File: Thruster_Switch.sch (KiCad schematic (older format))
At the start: 16 parts, among them P1 XT60, P2 XT60, P3 XT60, P4 XT60, Q1 BC817-40, Q2 IPD90P03P4L

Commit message: Fixed bugs from misunderstanding about Thruster, DVL, and Sonar switch biases.
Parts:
- removed C1: 1uF, Capacitors_SMD:C_0603, symbol C
- removed D1: MBR0530T3G, Diodes_SMD:D_SOD-123, symbol D
- removed Q1: BC817-40, TO_SOT_Packages_SMD:SOT-23, symbol BC817-40
- removed R1: 2.2k, Resistors_SMD:R_0603, symbol R
- removed R2: 330, Resistors_SMD:R_0603, symbol R
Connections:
- net labels removed: Hardware_Switch
- wire segments 32 -> 23
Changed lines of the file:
@@
 encoding utf-8
 Sheet 2 10
-Title ""
+Title "Thruster Switch"
 Date "2017-04-06"
 Rev "1.0.0"
@@
 L GND #PWR016
 U 1 1 58E0369B
-P 5250 4900
+P 6250 4800
 AR Path="/58E52973/58E0369B" Ref="#PWR016"  Part="1"
 AR Path="/58E62AD5/58E0369B" Ref="#PWR019"  Part="1"
 AR Path="/58E6D43E/58E0369B" Ref="#PWR020"  Part="1"
 AR Path="/58E0048C/58E0369B" Ref="#PWR021"  Part="1"
-F 0 "#PWR021" H 5250 4650 50  0001 C CNN
-F 1 "GND" H 5250 4750 50  0000 C CNN
-F 2 "" H 5250 4900 50  0001 C CNN
-F 3 "" H 5250 4900 50  0001 C CNN
-	1    5250 4900
-	1    0    0    -1
-$EndComp
-Text HLabel 3650 2300 0    60   Input ~ 0
+F 0 "#PWR016" H 6250 4550 50  0001 C CNN
+F 1 "GND" H 6250 4650 50  0000 C CNN
+F 2 "" H 6250 4800 50  0001 C CNN
+F 3 "" H 6250 4800 50  0001 C CNN
+	1    6250 4800
+	1    0    0    -1
+$EndComp
+Text HLabel 3700 2300 0    60   Input ~ 0
 +Power
-Text HLabel 3650 4050 0    60   Input ~ 0
+Text HLabel 3700 3050 0    60   Input ~ 0
 Software_Switch
-Text HLabel 3650 4650 0    60   Input ~ 0
-Hardware_Switch
 $Comp
 L XT60 P2
@@
 $EndComp
 $Comp
-L R R1
-U 1 1 58E4CD5F
-P 4000 4050
-AR Path="/58E52973/58E4CD5F" Ref="R1"  Part="1"
-AR Path="/58E62AD5/58E4CD5F" Ref="R16"  Part="1"
-AR Path="/58E6D43E/58E4CD5F" Ref="R21"  Part="1"
-AR Path="/58E0048C/58E4CD5F" Ref="R26"  Part="1"
-F 0 "R1" V 4080 4050 50  0000 C CNN
-F 1 "2.2k" V 4000 4050 50  0000 C CNN
-F 2 "Resistors_SMD:R_0603" V 3930 4050 50  0001 C CNN
-F 3 "" H 4000 4050 50  0001 C CNN
-	1    4000 4050
-	0    1    1    0
-$EndComp
-$Comp
-L BC817-40 Q1
-U 1 1 58E4F6EC
-P 5150 4050
-AR Path="/58E52973/58E4F6EC" Ref="Q1"  Part="1"
-AR Path="/58E62AD5/58E4F6EC" Ref="Q7"  Part="1"
-AR Path="/58E6D43E/58E4F6EC" Ref="Q9"  Part="1"
-AR Path="/58E0048C/58E4F6EC" Ref="Q11"  Part="1"
-F 0 "Q1" H 5350 4125 50  0000 L CNN
-F 1 "BC817-40" H 5350 4050 50  0000 L CNN
-F 2 "TO_SOT_Packages_SMD:SOT-23" H 5350 3975 50  0001 L CIN
-F 3 "" H 5150 4050 50  0001 L CNN
-	1    5150 4050
-	1    0    0    -1
-$EndComp
-$Comp
 L Fuse F1
 U 1 1 58E4FE30
@@
 	1    0    0    -1
 $EndComp
-$Comp
-L D D1
-U 1 1 58E515C3
-P 4250 4350
-AR Path="/58E52973/58E515C3" Ref="D1"  Part="1"
-AR Path="/58E62AD5/58E515C3" Ref="D8"  Part="1"
-AR Path="/58E6D43E/58E515C3" Ref="D11"  Part="1"
-AR Path="/58E0048C/58E515C3" Ref="D14"  Part="1"
-F 0 "D1" H 4250 4450 50  0000 C CNN
-F 1 "MBR0530T3G" H 4250 4250 50  0000 C CNN
-F 2 "Diodes_SMD:D_SOD-123" H 4250 4350 50  0001 C CNN
-F 3 "" H 4250 4350 50  0001 C CNN
-	1    4250 4350
-	0    -1   -1   0
-$EndComp
-$Comp
-L C C1
-U 1 1 58E53CD9
-P 4500 4350
-AR Path="/58E52973/58E53CD9" Ref="C1"  Part="1"
-AR Path="/58E62AD5/58E53CD9" Ref="C4"  Part="1"
-AR Path="/58E6D43E/58E53CD9" Ref="C5"  Part="1"
-AR Path="/58E0048C/58E53CD9" Ref="C6"  Part="1"
-F 0 "C1" H 4525 4450 50  0000 L CNN
-F 1 "1uF" H 4525 4250 50  0000 L CNN
-F 2 "Capacitors_SMD:C_0603" H 4538 4200 50  0001 C CNN
-F 3 "" H 4500 4350 50  0001 C CNN
-	1    4500 4350
-	1    0    0    -1
-$EndComp
 Wire Wire Line
 	6250 3850 8300 3850
@@
 	5700 3050 5950 3050
 Wire Wire Line
-	5400 3050 5250 3050
-Wire Wire Line
-	5250 2500 5250 3850
+	3700 3050 5400 3050
 Wire Wire Line
 	5250 2500 5400 2500
@@
 Wire Wire Line
 	6250 4450 6250 4300
-Connection ~ 6250 4750
 Connection ~ 6650 4750
 Wire Wire Line
@@
 Connection ~ 7200 4750
 Wire Wire Line
-	3850 4050 3650 4050
-Connection ~ 4250 4050
-Wire Wire Line
-	6250 4750 6250 4650
+	6250 4650 6250 4800
 Wire Wire Line
 	6250 3250 6250 3400
 Wire Wire Line
 	6250 3700 6250 4000
-Connection ~ 5250 4750
-Wire Wire Line
-	4250 4050 4250 4200
-Wire Wire Line
-	3650 4650 4250 4650
-Wire Wire Line
-	4250 4650 4250 4500
 $Comp
 L Q_PMOS_GDS Q2
@@
 	1    0    0    1
 $EndComp
-Wire Wire Line
-	5250 4250 5250 4900
-Wire Wire Line
-	3650 2300 6250 2300
-Wire Wire Line
-	4500 4750 8300 4750
-$Comp
-L R R2
-U 1 1 58E6316B
-P 4700 4050
-AR Path="/58E52973/58E6316B" Ref="R2"  Part="1"
-AR Path="/58E62AD5/58E6316B" Ref="R17"  Part="1"
-AR Path="/58E6D43E/58E6316B" Ref="R22"  Part="1"
-AR Path="/58E0048C/58E6316B" Ref="R27"  Part="1"
-F 0 "R2" V 4780 4050 50  0000 C CNN
-F 1 "330" V 4700 4050 50  0000 C CNN
-F 2 "Resistors_SMD:R_0603" V 4630 4050 50  0001 C CNN
-F 3 "" H 4700 4050 50  0001 C CNN
-	1    4700 4050
-	0    -1   -1   0
-$EndComp
-Wire Wire Line
-	4500 4200 4500 4050
-Wire Wire Line
-	4150 4050 4550 4050
-Wire Wire Line
-	4850 4050 4950 4050
-Wire Wire Line
-	4500 4500 4500 4750
-Connection ~ 4500 4050
 $Comp
 L D_Zener D2
@@
 	5850 2900 5850 3050
 Connection ~ 5850 3050
+Wire Wire Line
+	6250 4750 8300 4750
+Connection ~ 6250 4750
+Wire Wire Line
+	5250 3050 5250 2500
+Wire Wire Line
+	3700 2300 6250 2300
 $EndSCHEMATC

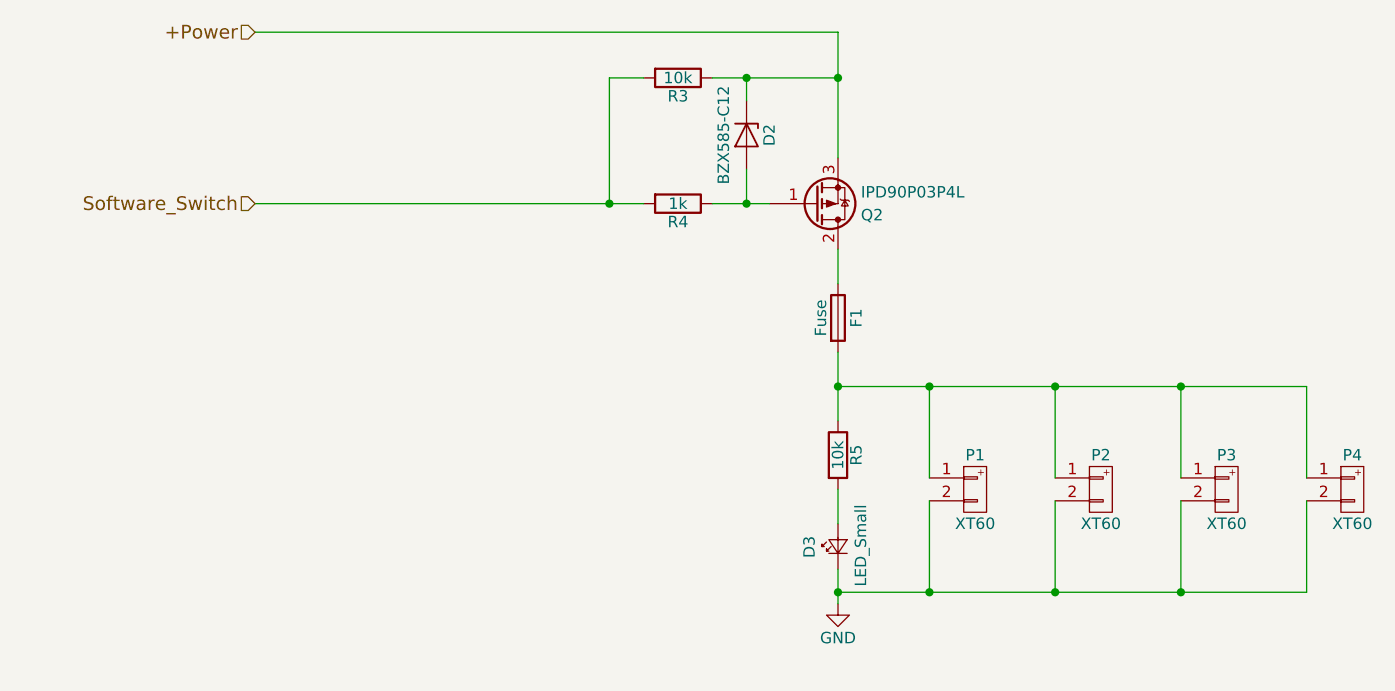
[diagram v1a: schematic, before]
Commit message: update footprint of JP1
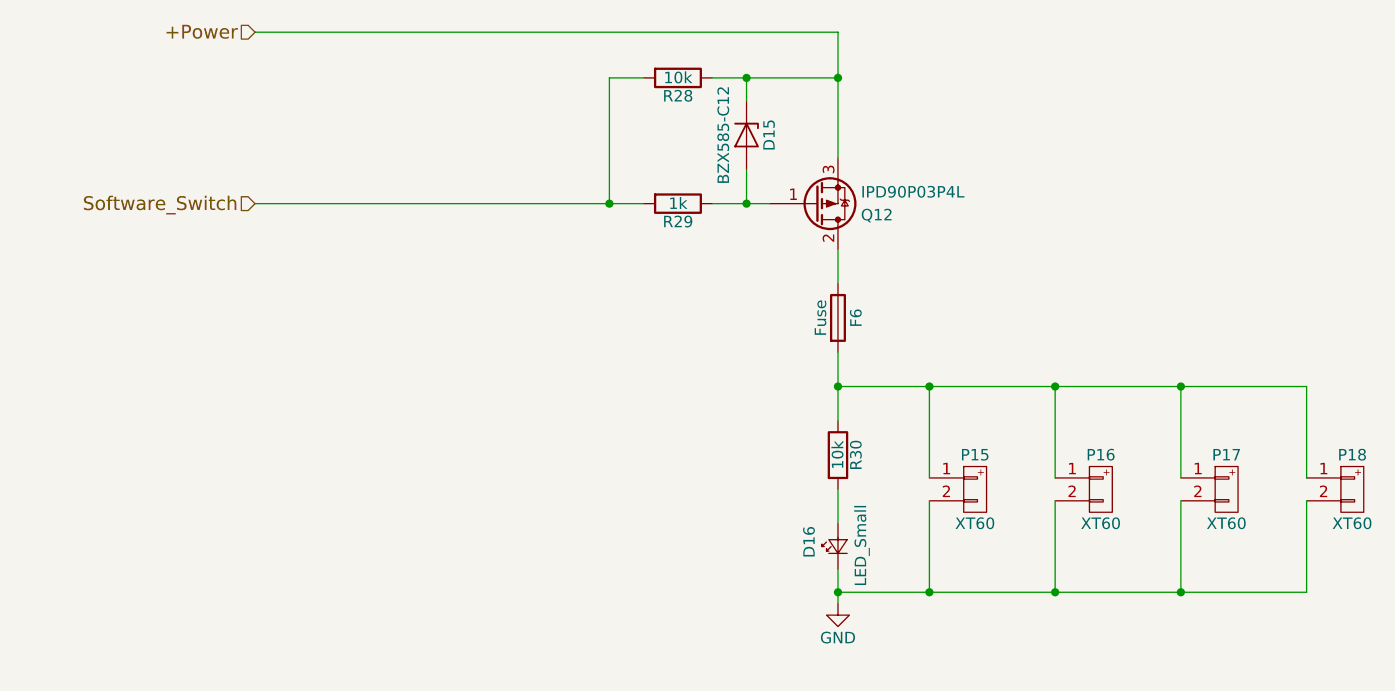
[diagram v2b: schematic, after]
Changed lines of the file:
@@
 LIBS:zeabus
 LIBS:ftdi
+LIBS:Power_Distributor-cache
 EELAYER 25 0
 EELAYER END
@@
 AR Path="/58E6D43E/58E019DD" Ref="P11"  Part="1"
 AR Path="/58E0048C/58E019DD" Ref="P15"  Part="1"
-F 0 "P1" H 6850 4450 50  0000 C CNN
+F 0 "P15" H 6850 4450 50  0000 C CNN
 F 1 "XT60" H 6850 4150 50  0000 C CNN
 F 2 "zeabus:XT60" H 6950 4050 60  0001 C CNN
@@
 AR Path="/58E6D43E/58E01A68" Ref="R25"  Part="1"
 AR Path="/58E0048C/58E01A68" Ref="R30"  Part="1"
-F 0 "R5" V 6330 4150 50  0000 C CNN
+F 0 "R30" V 6330 4150 50  0000 C CNN
 F 1 "10k" V 6250 4150 50  0000 C CNN
 F 2 "Resistors_SMD:R_0603" V 6180 4150 50  0001 C CNN
@@
 AR Path="/58E6D43E/58E01A8B" Ref="D13"  Part="1"
 AR Path="/58E0048C/58E01A8B" Ref="D16"  Part="1"
-F 0 "D3" H 6200 4675 50  0000 L CNN
+F 0 "D16" H 6200 4675 50  0000 L CNN
 F 1 "LED_Small" H 6075 4450 50  0000 L CNN
 F 2 "LEDs:LED_0603" V 6250 4550 50  0001 C CNN
@@
 AR Path="/58E6D43E/58E01FA8" Ref="R23"  Part="1"
 AR Path="/58E0048C/58E01FA8" Ref="R28"  Part="1"
-F 0 "R3" V 5630 2500 50  0000 C CNN
+F 0 "R28" V 5630 2500 50  0000 C CNN
 F 1 "10k" V 5550 2500 50  0000 C CNN
 F 2 "Resistors_SMD:R_0603" V 5480 2500 50  0001 C CNN
@@
 AR Path="/58E6D43E/58E01FFB" Ref="R24"  Part="1"
 AR Path="/58E0048C/58E01FFB" Ref="R29"  Part="1"
-F 0 "R4" V 5630 3050 50  0000 C CNN
+F 0 "R29" V 5630 3050 50  0000 C CNN
 F 1 "1k" V 5550 3050 50  0000 C CNN
 F 2 "Resistors_SMD:R_0603" V 5480 3050 50  0001 C CNN
@@
 $EndComp
 $Comp
-L GND #PWR016
+L GND #PWR12
 U 1 1 58E0369B
 P 6250 4800
-AR Path="/58E52973/58E0369B" Ref="#PWR016"  Part="1"
-AR Path="/58E62AD5/58E0369B" Ref="#PWR019"  Part="1"
-AR Path="/58E6D43E/58E0369B" Ref="#PWR020"  Part="1"
-AR Path="/58E0048C/58E0369B" Ref="#PWR021"  Part="1"
-F 0 "#PWR016" H 6250 4550 50  0001 C CNN
+AR Path="/58E52973/58E0369B" Ref="#PWR12"  Part="1"
+AR Path="/58E62AD5/58E0369B" Ref="#PWR15"  Part="1"
+AR Path="/58E6D43E/58E0369B" Ref="#PWR16"  Part="1"
+AR Path="/58E0048C/58E0369B" Ref="#PWR17"  Part="1"
+F 0 "#PWR17" H 6250 4550 50  0001 C CNN
 F 1 "GND" H 6250 4650 50  0000 C CNN
 F 2 "" H 6250 4800 50  0001 C CNN
@@
 AR Path="/58E6D43E/58E0D2A0" Ref="P12"  Part="1"
 AR Path="/58E0048C/58E0D2A0" Ref="P16"  Part="1"
-F 0 "P2" H 7400 4450 50  0000 C CNN
+F 0 "P16" H 7400 4450 50  0000 C CNN
 F 1 "XT60" H 7400 4150 50  0000 C CNN
 F 2 "zeabus:XT60" H 7500 4050 60  0001 C CNN
@@
 AR Path="/58E6D43E/58E0D2E8" Ref="P13"  Part="1"
 AR Path="/58E0048C/58E0D2E8" Ref="P17"  Part="1"
-F 0 "P3" H 7950 4450 50  0000 C CNN
+F 0 "P17" H 7950 4450 50  0000 C CNN
 F 1 "XT60" H 7950 4150 50  0000 C CNN
 F 2 "zeabus:XT60" H 8050 4050 60  0001 C CNN
@@
 AR Path="/58E6D43E/58E0D33F" Ref="P14"  Part="1"
 AR Path="/58E0048C/58E0D33F" Ref="P18"  Part="1"
-F 0 "P4" H 8500 4450 50  0000 C CNN
+F 0 "P18" H 8500 4450 50  0000 C CNN
 F 1 "XT60" H 8500 4150 50  0000 C CNN
 F 2 "zeabus:XT60" H 8600 4050 60  0001 C CNN
@@
 AR Path="/58E6D43E/58E4FE30" Ref="F5"  Part="1"
 AR Path="/58E0048C/58E4FE30" Ref="F6"  Part="1"
-F 0 "F1" V 6330 3550 50  0000 C CNN
+F 0 "F6" V 6330 3550 50  0000 C CNN
 F 1 "Fuse" V 6175 3550 50  0000 C CNN
 F 2 "zeabus:FUSE_AUTO" V 6180 3550 50  0001 C CNN
@@
 AR Path="/58E6D43E/58E51C6A" Ref="Q10"  Part="1"
 AR Path="/58E0048C/58E51C6A" Ref="Q12"  Part="1"
-F 0 "Q2" H 6350 3100 50  0000 L CNN
+F 0 "Q12" H 6350 3100 50  0000 L CNN
 F 1 "IPD90P03P4L" H 6350 3000 50  0000 L CNN
 F 2 "TO_SOT_Packages_SMD:TO-252-2Lead" H 6350 3150 50  0001 C CNN
@@
 AR Path="/58E6D43E/58E6427A" Ref="D12"  Part="1"
 AR Path="/58E0048C/58E6427A" Ref="D15"  Part="1"
-F 0 "D2" H 5850 2850 50  0000 C CNN
+F 0 "D15" H 5850 2850 50  0000 C CNN
 F 1 "BZX585-C12" H 5850 2650 50  0000 C CNN
 F 2 "Diodes_SMD:D_SOD-523" H 5850 2750 50  0001 C CNN

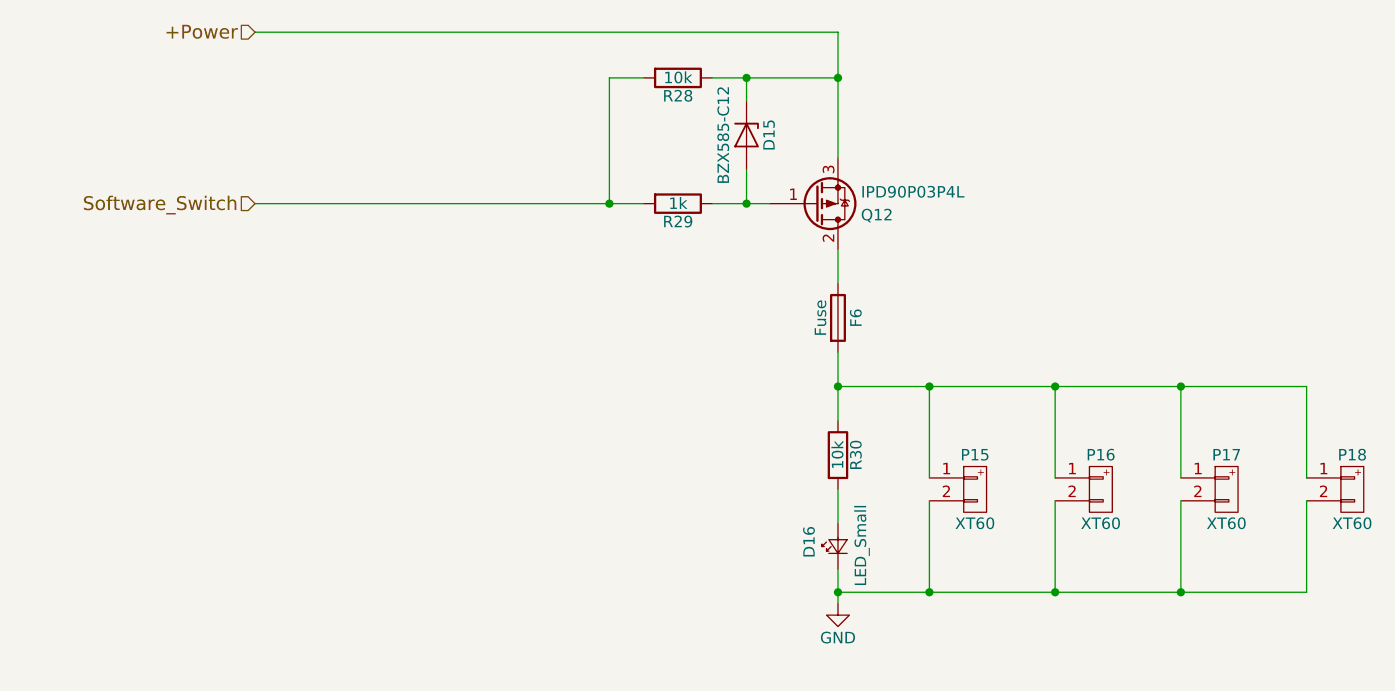
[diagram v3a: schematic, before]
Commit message: Draw Lamp Supply sch with "I6A24014A033V"
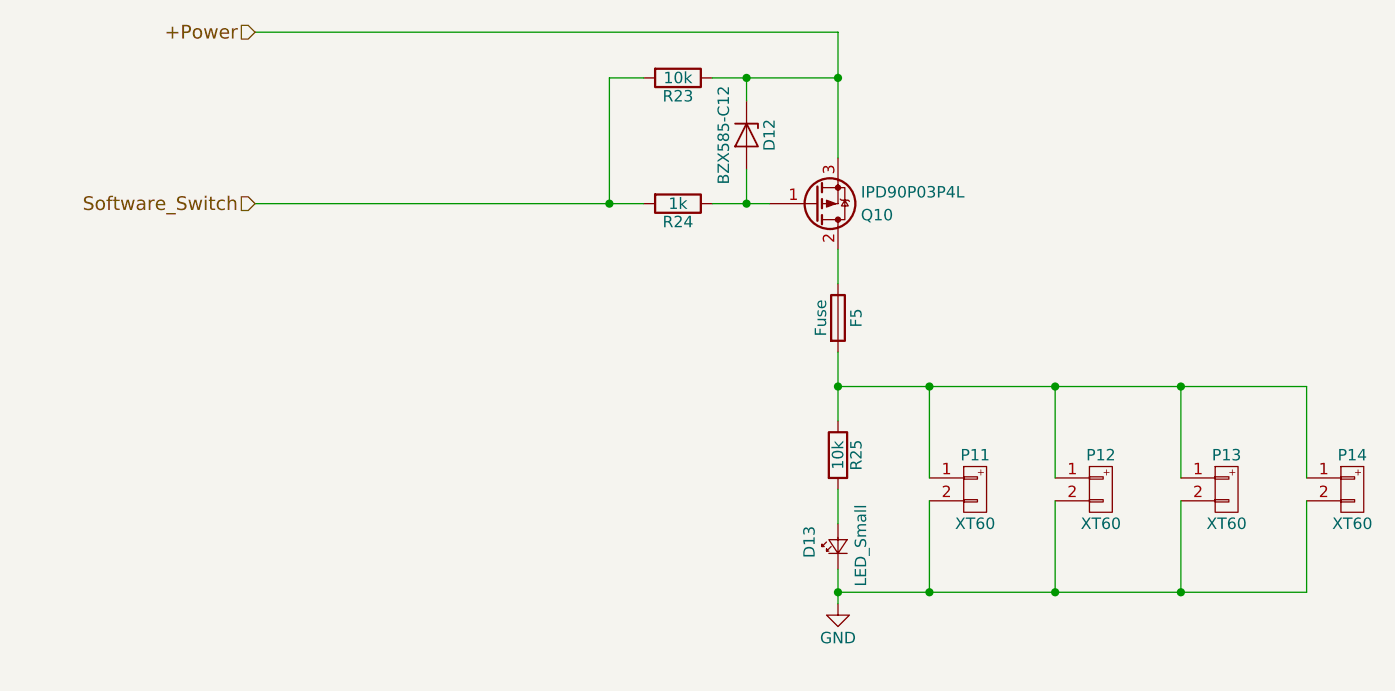
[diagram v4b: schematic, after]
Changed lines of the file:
@@
 $Descr A4 11693 8268
 encoding utf-8
-Sheet 7 10
+Sheet 6 10
 Title "Thruster Switch"
 Date "2017-04-06"
@@
 AR Path="/58E6D43E/58E019DD" Ref="P11"  Part="1"
 AR Path="/58E0048C/58E019DD" Ref="P15"  Part="1"
-F 0 "P15" H 6850 4450 50  0000 C CNN
+F 0 "P11" H 6850 4450 50  0000 C CNN
 F 1 "XT60" H 6850 4150 50  0000 C CNN
 F 2 "zeabus:XT60" H 6950 4050 60  0001 C CNN
@@
 AR Path="/58E6D43E/58E01A68" Ref="R25"  Part="1"
 AR Path="/58E0048C/58E01A68" Ref="R30"  Part="1"
-F 0 "R30" V 6330 4150 50  0000 C CNN
+F 0 "R25" V 6330 4150 50  0000 C CNN
 F 1 "10k" V 6250 4150 50  0000 C CNN
 F 2 "Resistors_SMD:R_0603" V 6180 4150 50  0001 C CNN
@@
 AR Path="/58E6D43E/58E01A8B" Ref="D13"  Part="1"
 AR Path="/58E0048C/58E01A8B" Ref="D16"  Part="1"
-F 0 "D16" H 6200 4675 50  0000 L CNN
+F 0 "D13" H 6200 4675 50  0000 L CNN
 F 1 "LED_Small" H 6075 4450 50  0000 L CNN
 F 2 "LEDs:LED_0603" V 6250 4550 50  0001 C CNN
@@
 AR Path="/58E6D43E/58E01FA8" Ref="R23"  Part="1"
 AR Path="/58E0048C/58E01FA8" Ref="R28"  Part="1"
-F 0 "R28" V 5630 2500 50  0000 C CNN
+F 0 "R23" V 5630 2500 50  0000 C CNN
 F 1 "10k" V 5550 2500 50  0000 C CNN
 F 2 "Resistors_SMD:R_0603" V 5480 2500 50  0001 C CNN
@@
 AR Path="/58E6D43E/58E01FFB" Ref="R24"  Part="1"
 AR Path="/58E0048C/58E01FFB" Ref="R29"  Part="1"
-F 0 "R29" V 5630 3050 50  0000 C CNN
+F 0 "R24" V 5630 3050 50  0000 C CNN
 F 1 "1k" V 5550 3050 50  0000 C CNN
 F 2 "Resistors_SMD:R_0603" V 5480 3050 50  0001 C CNN
@@
 AR Path="/58E6D43E/58E0D2A0" Ref="P12"  Part="1"
 AR Path="/58E0048C/58E0D2A0" Ref="P16"  Part="1"
-F 0 "P16" H 7400 4450 50  0000 C CNN
+F 0 "P12" H 7400 4450 50  0000 C CNN
 F 1 "XT60" H 7400 4150 50  0000 C CNN
 F 2 "zeabus:XT60" H 7500 4050 60  0001 C CNN
@@
 AR Path="/58E6D43E/58E0D2E8" Ref="P13"  Part="1"
 AR Path="/58E0048C/58E0D2E8" Ref="P17"  Part="1"
-F 0 "P17" H 7950 4450 50  0000 C CNN
+F 0 "P13" H 7950 4450 50  0000 C CNN
 F 1 "XT60" H 7950 4150 50  0000 C CNN
 F 2 "zeabus:XT60" H 8050 4050 60  0001 C CNN
@@
 AR Path="/58E6D43E/58E0D33F" Ref="P14"  Part="1"
 AR Path="/58E0048C/58E0D33F" Ref="P18"  Part="1"
-F 0 "P18" H 8500 4450 50  0000 C CNN
+F 0 "P14" H 8500 4450 50  0000 C CNN
 F 1 "XT60" H 8500 4150 50  0000 C CNN
 F 2 "zeabus:XT60" H 8600 4050 60  0001 C CNN
@@
 AR Path="/58E6D43E/58E4FE30" Ref="F5"  Part="1"
 AR Path="/58E0048C/58E4FE30" Ref="F6"  Part="1"
-F 0 "F6" V 6330 3550 50  0000 C CNN
+F 0 "F5" V 6330 3550 50  0000 C CNN
 F 1 "Fuse" V 6175 3550 50  0000 C CNN
 F 2 "zeabus:FUSE_AUTO" V 6180 3550 50  0001 C CNN
@@
 AR Path="/58E6D43E/58E51C6A" Ref="Q10"  Part="1"
 AR Path="/58E0048C/58E51C6A" Ref="Q12"  Part="1"
-F 0 "Q12" H 6350 3100 50  0000 L CNN
+F 0 "Q10" H 6350 3100 50  0000 L CNN
 F 1 "IPD90P03P4L" H 6350 3000 50  0000 L CNN
 F 2 "TO_SOT_Packages_SMD:TO-252-2Lead" H 6350 3150 50  0001 C CNN
@@
 AR Path="/58E6D43E/58E6427A" Ref="D12"  Part="1"
 AR Path="/58E0048C/58E6427A" Ref="D15"  Part="1"
-F 0 "D15" H 5850 2850 50  0000 C CNN
+F 0 "D12" H 5850 2850 50  0000 C CNN
 F 1 "BZX585-C12" H 5850 2650 50  0000 C CNN
 F 2 "Diodes_SMD:D_SOD-523" H 5850 2750 50  0001 C CNN
